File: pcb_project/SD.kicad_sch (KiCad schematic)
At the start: 21 parts, among them J6 MEM2052-00-195-00-A, U10 TPD1E1B04DPYT, U11 TPD1E1B04DPYT, U12 TPD1E1B04DPYT, U13 TPD1E1B04DPYT, U5 TPD1E1B04DPYT, U6 TPD1E1B04DPYT

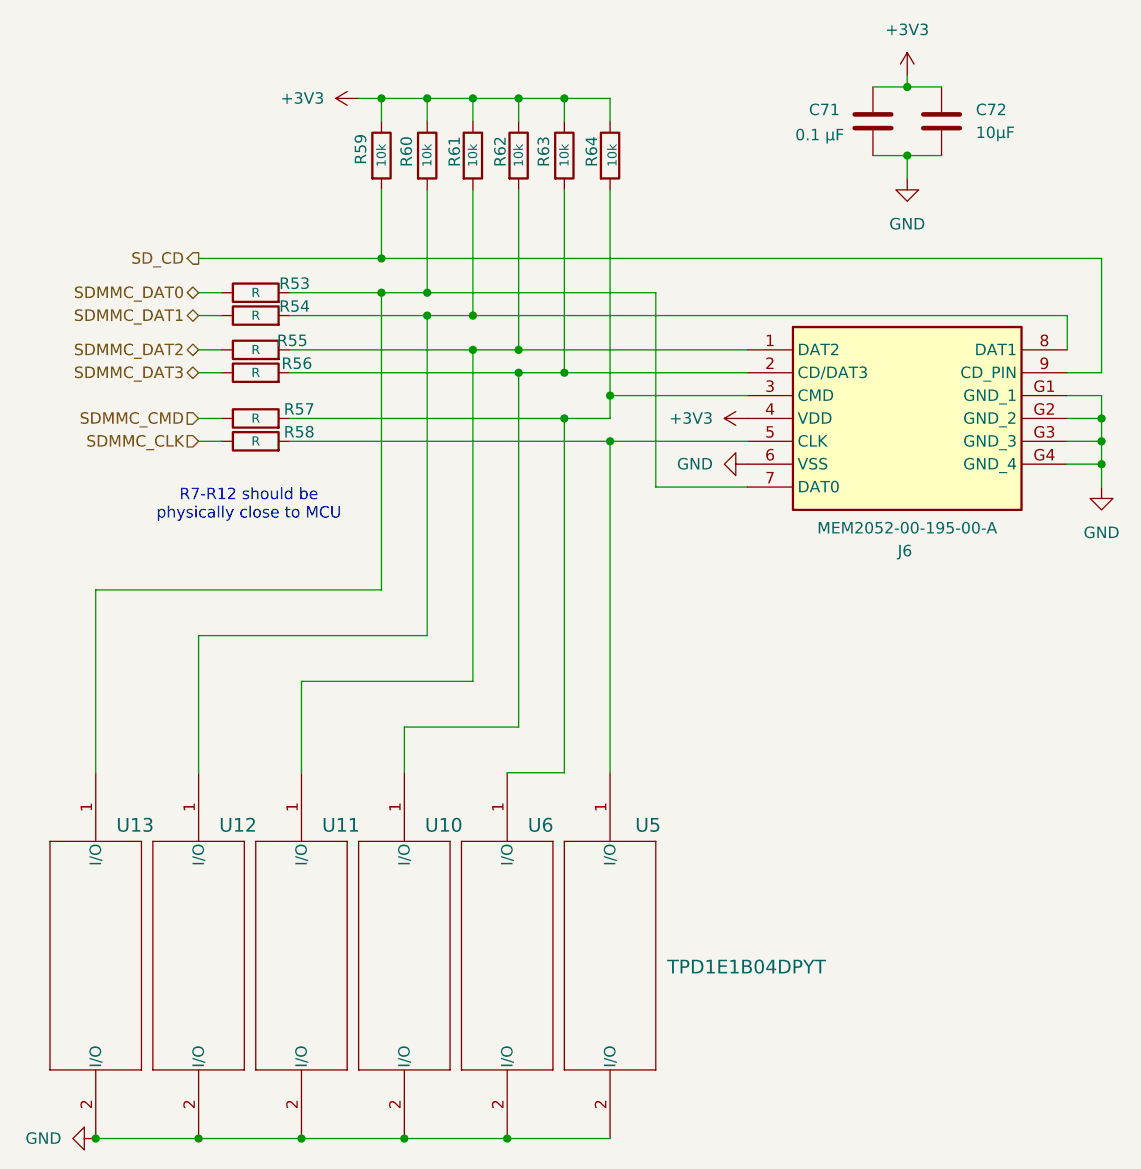
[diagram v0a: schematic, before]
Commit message: Fix DRC errors
- Remove ESD as they do not work
- Increase zone priotity for overlapping zones
- Connect some unconnected pads
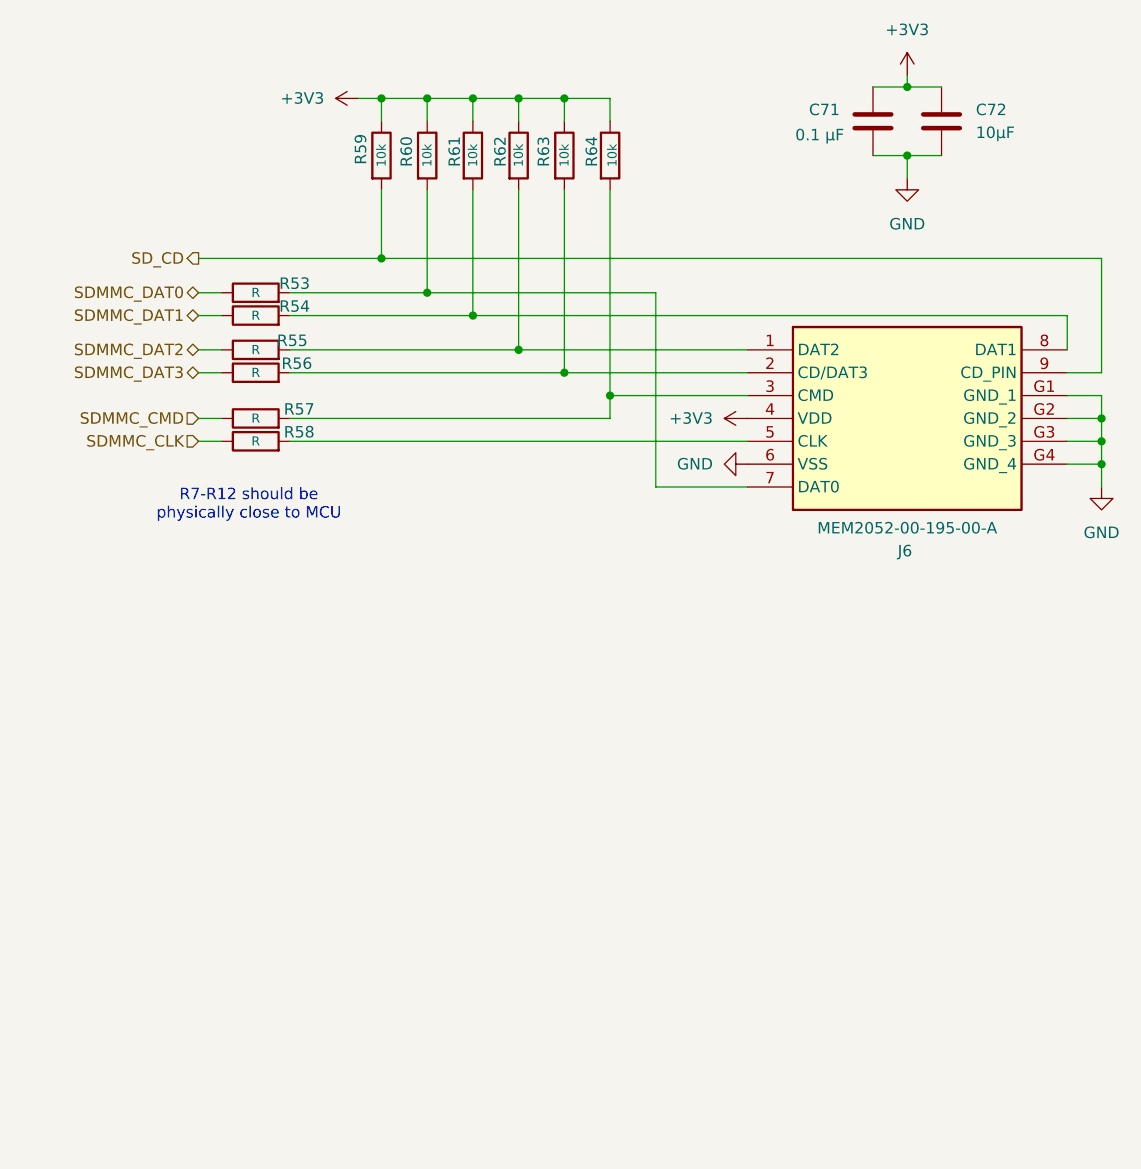
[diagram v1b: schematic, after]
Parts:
- removed U10, U11, U12, U13, U5, U6: TPD1E1B04DPYT, Project_Footprints:DPY2_TEX, symbol 2025-09-27_10-20-59:TPD1E1B04DPYT
